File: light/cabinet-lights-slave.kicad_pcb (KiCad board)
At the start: 2 copper layers, 50 x 50 mm, 15 parts, among them J1 NORTH, J2 EAST, J3 SOUTH, J4 WEST, Q1 NX7002AK, Q2 NTR1P02T1G

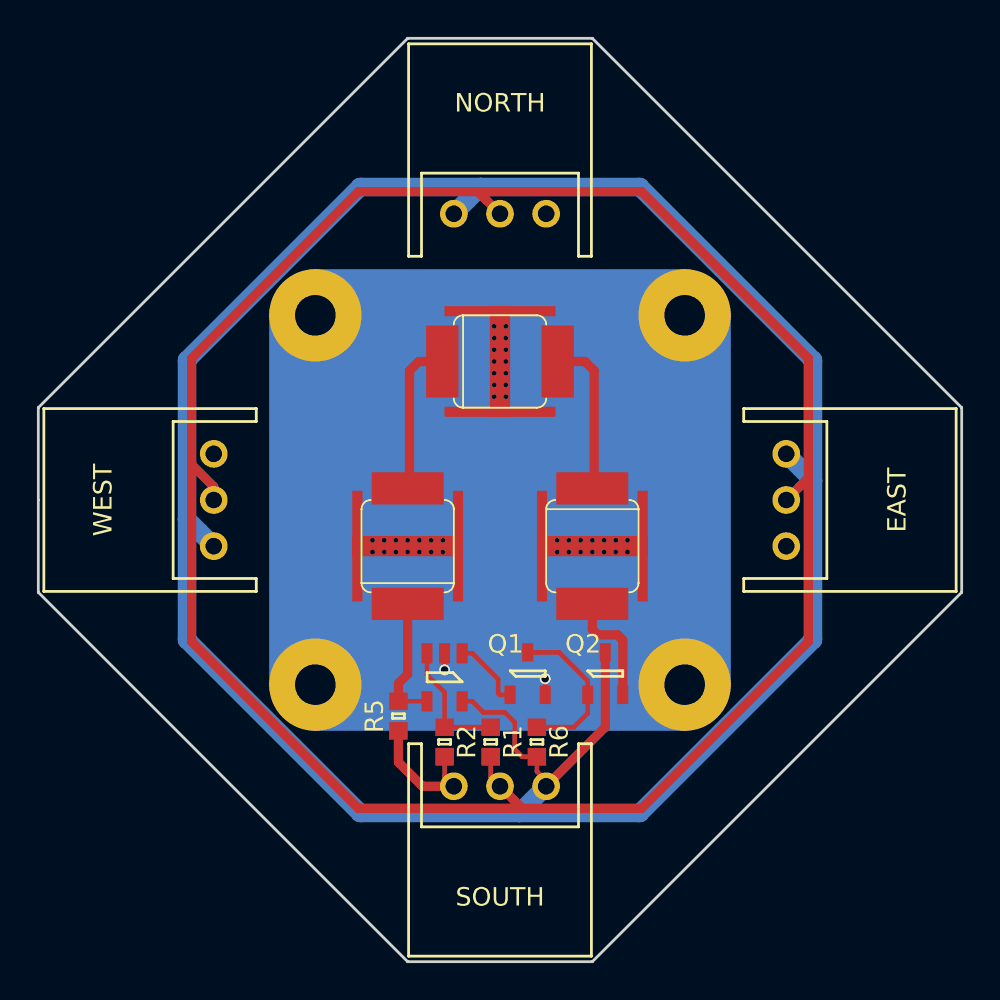
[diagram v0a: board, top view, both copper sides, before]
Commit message: Models for LED and JST conn, slight PCB shuffle
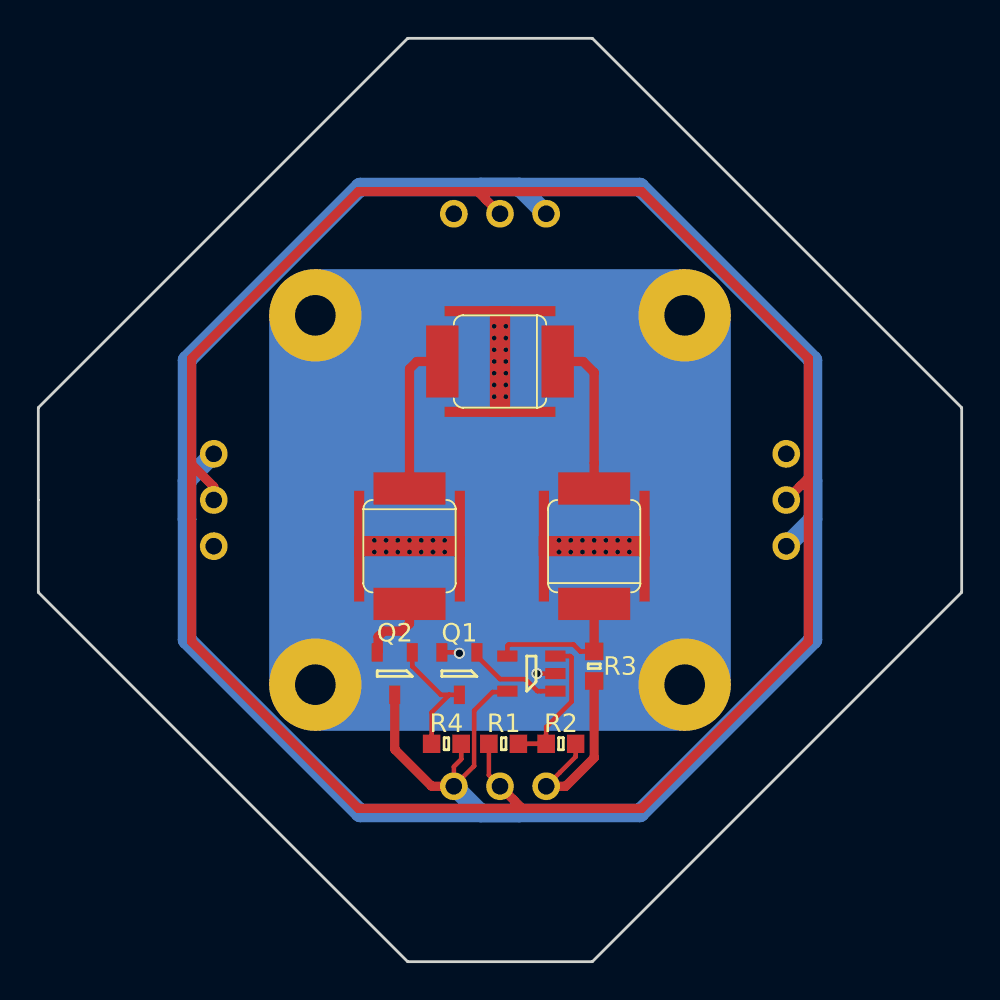
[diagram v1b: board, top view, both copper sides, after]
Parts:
- removed R5: 0R24, agg:0603
- removed R6: 1k, agg:0603
- added R3: 0R24, agg:0603, F.Cu at (60.1, 64.0)
- added R4: 1k, agg:0603, F.Cu at (52.1, 68.2)
- J1, J2, J3, J4: footprint parts:S3D-XH-A -> parts:S3B-XH-A; moved to B.Cu
- moved Q2 11.4 mm to (49.3, 64.4), turned to 270 degrees
- moved D3 10.1 mm to (60.1, 57.5)
- moved D1 9.90 mm to (50.1, 57.5)
- moved R2 6.30 mm to (58.3, 68.2), turned to 180 degrees
- moved OP?1 4.70 mm to (56.7, 64.4), turned to 180 degrees
- moved Q1 3.70 mm to (52.8, 64.4), turned to 270 degrees
- moved J1 2.50 mm to (57.5, 39.5), turned to 180 degrees
- moved J2 2.50 mm to (70.5, 57.5), turned to 90 degrees
- moved J3 2.50 mm to (52.5, 70.5), turned to 0 degrees
- moved J4 2.50 mm to (39.5, 52.5), turned to 270 degrees
- moved R1 0.71 mm to (55.2, 68.2), turned to 180 degrees
- turned D2 to 180 degrees
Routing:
- net +12V: track 138.4 -> 146.5 mm
- net GND: track 8.82 -> 12.6 mm
- net Net-(D1-Pad2): track 6.64 -> 3.94 mm
- net Net-(Q1-Pad3): track 8.91 -> 6.99 mm
- net /SENSE: track 7.03 -> 8.43 mm
- net Net-(OP?1-Pad1): track 3.97 -> 5.24 mm
- net /DIM/100: track 6.89 -> 7.65 mm
- net /DIM: track 121.8 -> 122.5 mm
